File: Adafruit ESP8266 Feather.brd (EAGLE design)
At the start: 50.8 x 22.9 mm, 40 parts, among them IC1 CP2104, Q1 mmbt2222, Q2 mmbt2222, SW2 KMR2, U2 SPX3819, U3 MCP73831T-2ACI/OT, X1 JSTPH, X2 ESP-12, X4 20329

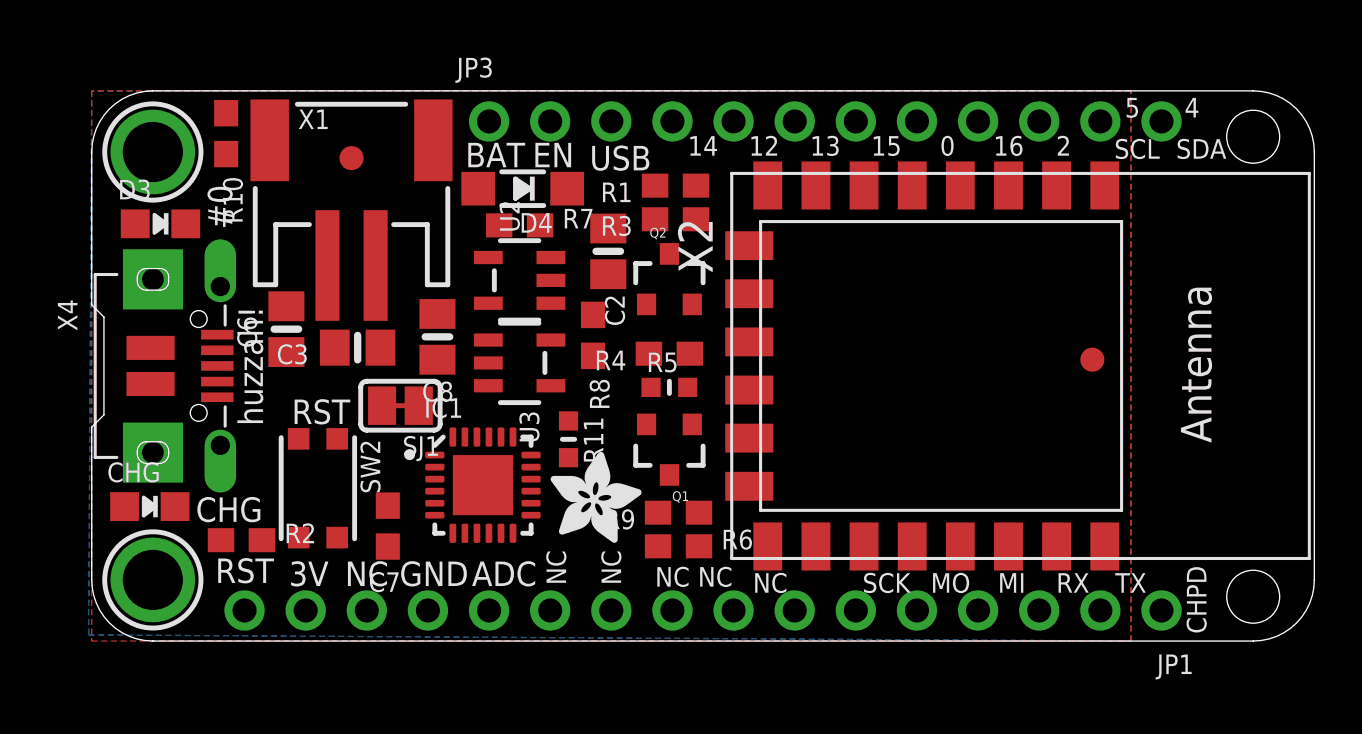
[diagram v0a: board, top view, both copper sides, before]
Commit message: Finished Schematic: CP2104 + SPX3819 + MCP73831T-2ACI/OT + KMR2(Reset)
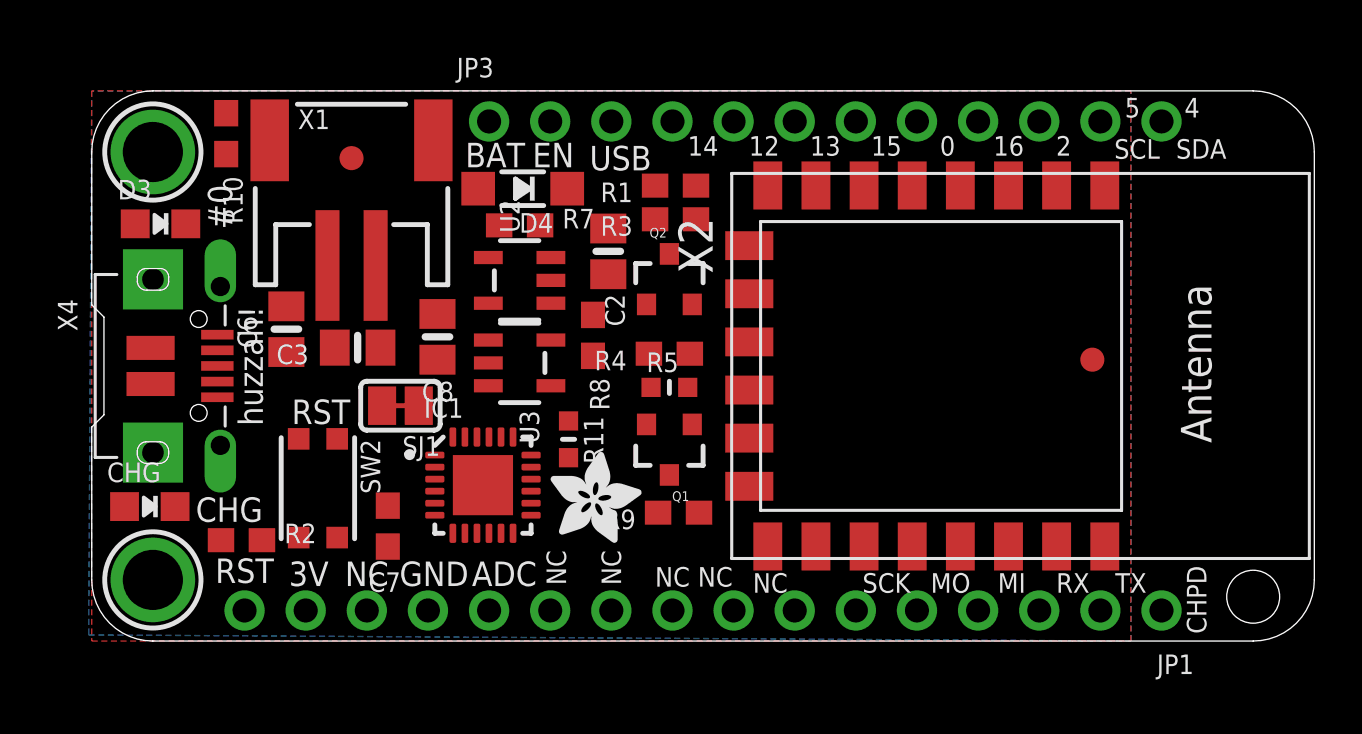
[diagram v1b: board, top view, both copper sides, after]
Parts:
- removed R6: 4.7K, microbuilder:0603-NO
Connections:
- removed net IN: U2.1
- removed net REGIN: IC1.7
- removed net VDD: IC1.6, U3.4
- removed net VIO: IC1.5
- removed net VSS: U3.2
- new net DTR: IC1.23
- new net EN: R7.1, U2.3
- new net GPIO0: R10.1
- new net N$1: CHG.C, R2.1
- new net N$2: IC1.3, X4.D+
- new net N$3: R2.2, U3.1
- new net N$4: R8.1, U3.5
- new net N$6: IC1.4, X4.D-
- new net N$7: SJ1.1, U3.3
- new net RTS: IC1.19
- new net TXD: IC1.20
- new net USB_RX: IC1.21
- new net VCC: X2.8
- net 3.3V: now also C2.1, C7.1, C8.1, D3.A, IC1.5, IC1.6, IC1.7, U2.5; no longer X2.8
- net GND: now also C2.2, C3.2, C6.2, C7.2, C8.2, R8.2, SW2.A, SW2.A', U3.2, X1.1
- net RESET: now also R3.1
- net VBAT: now also C3.1, D4.A, SJ1.2, X1.2; no longer U3.3
- net VBUS: now also C6.1, CHG.A, D4.C, R7.2, U2.1, U3.4

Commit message: Schematic: ESP8266 + (JP1 + JP3 I/O Headers)
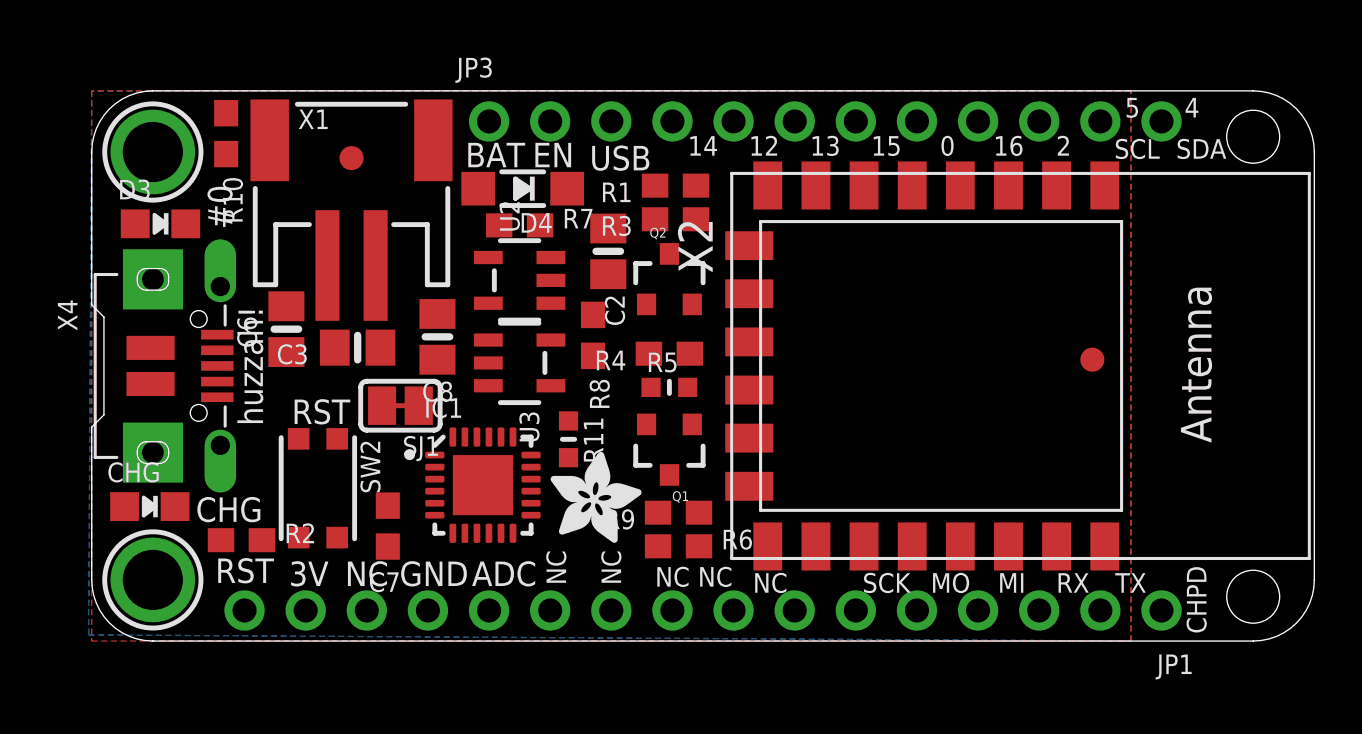
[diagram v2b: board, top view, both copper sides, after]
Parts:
- added R6: 4.7K, microbuilder:0603-NO
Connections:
- removed net VCC: X2.8
- new net ADC: JP1.12, X2.2
- new net CH_PD: JP1.1, R1.1, X2.3
- new net GPIO12/MISO: JP1.4, JP3.5, X2.6
- new net GPIO13/MOSI: JP1.5, JP3.6, X2.7
- new net GPIO14/SCK: JP1.6, JP3.4, X2.5
- new net GPIO15: JP3.7, R6.2, X2.10
- new net GPIO16: JP3.9, X2.4
- new net GPIO2: JP3.10, R9.1, X2.11
- new net GPIO4/SDA: JP3.12, X2.13
- new net GPIO5/SCL: JP3.11, X2.14
- new net N$12: Q1.1, R4.2
- new net N$13: Q2.1, R5.2
- new net RXD: JP1.3, R11.2, X2.15
- net 3.3V: now also JP1.15, R1.2, R9.2, X2.8
- net DTR: now also Q2.2, R4.1
- net EN: now also JP3.2
- net GND: now also JP1.13, R6.1
- net GPIO0: now also JP3.8, Q2.3, X2.12
- net RESET: now also JP1.16, Q1.3, X2.1
- net RTS: now also Q1.2, R5.1
- net TXD: now also JP1.2, X2.16
- net USB_RX: now also R11.1
- net VBAT: now also JP3.1
- net VBUS: now also JP3.3

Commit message: Traces Top: ESP8266 Unrouted
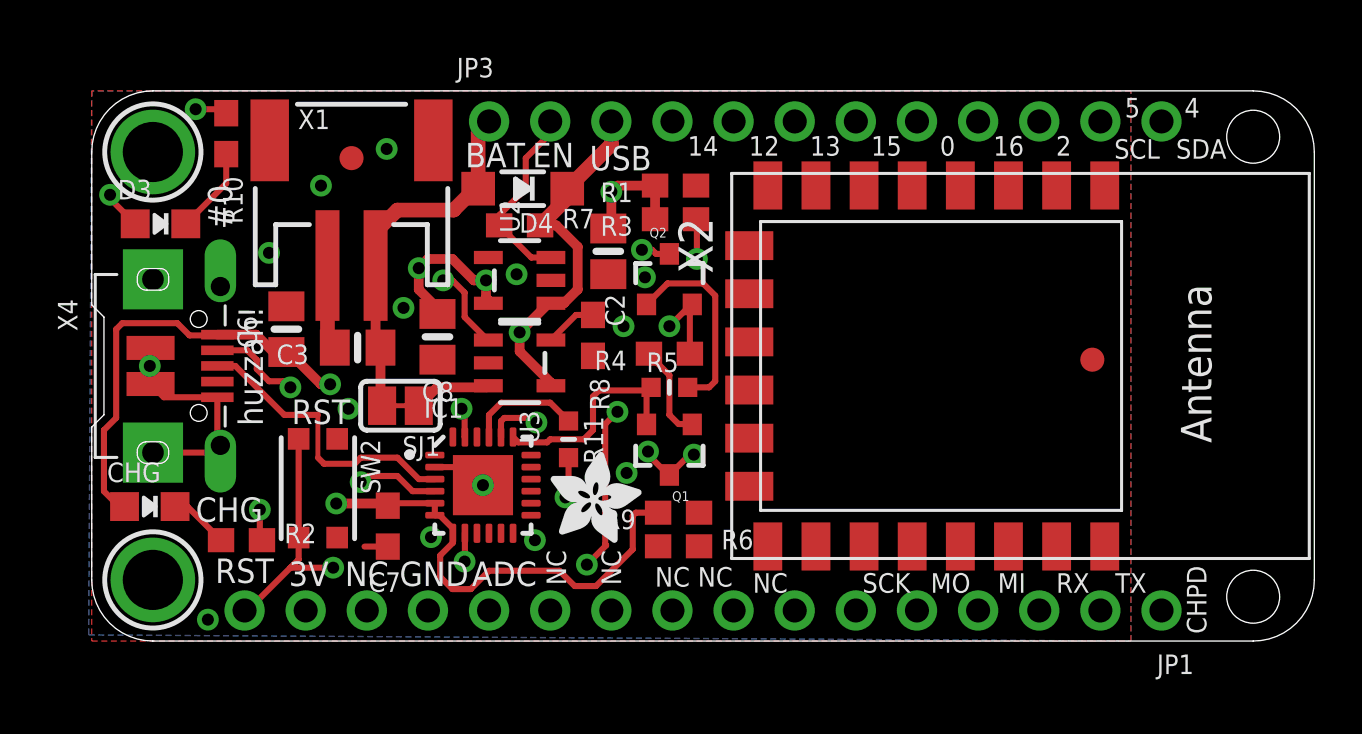
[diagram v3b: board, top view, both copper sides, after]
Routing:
- net VBUS: track 0.00 -> 34.5 mm, vias 0 -> 3
- net 3.3V: track 0.00 -> 32.9 mm, vias 0 -> 5
- net GND: track 0.00 -> 16.7 mm, vias 0 -> 14
- net VBAT: track 0.00 -> 15.5 mm
- net RESET: track 0.00 -> 14.3 mm, vias 0 -> 4
- net N$2: track 0.00 -> 12.2 mm
- net GPIO0: track 0.00 -> 9.46 mm, vias 0 -> 4
- net RTS: track 0.00 -> 9.03 mm
- net N$13: track 0.00 -> 8.23 mm
- net EN: track 0.00 -> 7.90 mm
- net N$6: track 0.00 -> 7.34 mm, vias 0 -> 2
- net N$3: track 0.00 -> 4.80 mm, vias 0 -> 2
- net USB_RX: track 0.00 -> 4.75 mm
- net DTR: track 0.00 -> 4.71 mm, vias 0 -> 2
- net N$12: track 0.00 -> 4.01 mm
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
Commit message: Feather .Brd: minor adjustments
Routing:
- net GPIO0: track 9.46 -> 77.7 mm, vias 4 -> 6
- net RESET: track 14.3 -> 74.4 mm, vias 4 -> 5
- net 3.3V: track 32.9 -> 86.4 mm
- net ADC: track 0.00 -> 44.7 mm, vias 0 -> 1
- net CH_PD: track 0.71 -> 42.4 mm, vias 0 -> 2
- net GPIO14/SCK: track 0.00 -> 34.1 mm, vias 0 -> 1
- net GPIO12/MISO: track 0.00 -> 32.8 mm, vias 0 -> 2
- net TXD: track 2.26 -> 33.3 mm, vias 1 -> 2
- net GPIO2: track 0.13 -> 30.7 mm, vias 0 -> 2
- net RXD: track 1.70 -> 27.6 mm, vias 1 -> 2
- net GPIO15: track 0.29 -> 25.9 mm, vias 0 -> 1
- net GPIO13/MOSI: track 0.00 -> 25.3 mm, vias 0 -> 2
- net VBUS: track 34.5 -> 56.3 mm
- net GPIO4/SDA: track 0.00 -> 21.6 mm, vias 0 -> 1
- net GPIO5/SCL: track 0.00 -> 20.3 mm, vias 0 -> 1
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
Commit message: Feather .Brd: completed the layout design
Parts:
- removed IC1: CP2104, microbuilder:QFN24_4MM_SMSC
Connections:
- net 3.3V: no longer IC1.5, IC1.6, IC1.7
- net CH_PD: no longer X2.3
- net DTR: no longer IC1.23
- net GND: no longer IC1.2, IC1.THERM
- net N$2: no longer IC1.3
- net N$6: no longer IC1.4
- net RTS: no longer IC1.19
- net TXD: no longer IC1.20
- net USB_RX: no longer IC1.21
- net VBUS: no longer IC1.8
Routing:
- net CH_PD: track 42.4 -> 31.5 mm
- net 3.3V: track 86.4 -> 82.7 mm
- net GND: track 16.7 -> 15.0 mm, vias 16 -> 15
- net VBUS: track 56.3 -> 55.1 mm
- net N$6: track 12.5 -> 11.6 mm
- net USB_RX: track 4.75 -> 3.83 mm
- net N$2: track 12.2 -> 11.6 mm
- net TXD: track 33.3 -> 32.7 mm
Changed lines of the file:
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@@
 <attribute name="VALUE" x="5.08" y="19.05" size="0.8128" layer="27" font="vector" ratio="10" rot="R270"/>
-</element>
-<element name="IC1" library="microbuilder" package="QFN24_4MM_SMSC" value="CP2104" x="16.256" y="6.477" smashed="yes">
-<attribute name="NAME" x="13.806" y="9.277" size="0.8128" layer="25" ratio="18"/>
-<attribute name="VALUE" x="14.137" y="5.105" size="0.8128" layer="27" ratio="10"/>
 </element>
 <element name="X4" library="microbuilder" package="4UCONN_20329_V2" value="20329" x="4.445" y="11.43" smashed="yes" rot="R270">
@@
 <contactref element="SW2" pad="A"/>
 <contactref element="SW2" pad="A'"/>
-<contactref element="IC1" pad="2"/>
 <contactref element="X4" pad="SPRT@1"/>
 <contactref element="X4" pad="SPRT@2"/>
@@
 <contactref element="X4" pad="GND"/>
 <contactref element="C2" pad="2"/>
-<contactref element="IC1" pad="THERM"/>
-<wire x1="16.002" y1="7.227" x2="14.256" y2="7.227" width="0.254" layer="1"/>
 <via x="10.668" y="9.652" extent="1-16" drill="0.5"/>
-<via x="16.256" y="6.477" extent="1-16" drill="0.5"/>
 <via x="18.415" y="4.191" extent="1-16" drill="0.5"/>
 <via x="22.225" y="6.985" extent="1-16" drill="0.5"/>
@@
 <wire x1="14.366" y1="11.69" x2="14.366" y2="11.572" width="0.4064" layer="1"/>
 <wire x1="14.366" y1="11.572" x2="14.224" y2="11.43" width="0.4064" layer="1"/>
+<wire x1="21.463" y1="15.2425" x2="22.987" y2="15.113" width="0" layer="19" extent="1-1"/>
+<wire x1="22.098" y1="13.081" x2="22.987" y2="15.113" width="0" layer="19" extent="1-1"/>
+<wire x1="20.828" y1="11.85" x2="22.098" y2="13.081" width="0" layer="19" extent="1-1"/>
+<wire x1="19.0801" y1="14.986" x2="21.463" y2="15.2425" width="0" layer="19" extent="1-1"/>
+<wire x1="17.653" y1="15.24" x2="19.0801" y2="14.986" width="0" layer="19" extent="1-1"/>
+<wire x1="16.4799" y1="11.557" x2="17.653" y2="15.24" width="0" layer="19" extent="1-1"/>
+<wire x1="14.366" y1="11.69" x2="16.4799" y2="11.557" width="0" layer="19" extent="1-1"/>
+<wire x1="12.954" y1="13.843" x2="14.366" y2="11.69" width="0" layer="19" extent="1-1"/>
+<wire x1="10.099" y1="12.192" x2="12.954" y2="13.843" width="0" layer="19" extent="1-1"/>
+<wire x1="8.088" y1="13.909" x2="9.795" y2="15.604" width="0" layer="19" extent="1-1"/>
+<wire x1="7.366" y1="16.129" x2="8.088" y2="13.909" width="0" layer="19" extent="1-1"/>
+<wire x1="5.345" y1="14.73" x2="7.366" y2="16.129" width="0" layer="19" extent="1-1"/>
+<wire x1="10.668" y1="9.652" x2="10.099" y2="12.192" width="0" layer="19" extent="1-1"/>
+<wire x1="10.198" y1="8.4" x2="10.668" y2="9.652" width="0" layer="19" extent="1-1"/>
+<wire x1="2.545" y1="15.03" x2="5.345" y2="14.73" width="0" layer="19" extent="1-1"/>
+<wire x1="2.445" y1="12.18" x2="2.545" y2="15.03" width="0" layer="19" extent="1-1"/>
+<wire x1="2.413" y1="11.43" x2="2.445" y2="12.18" width="0" layer="19" extent="1-1"/>
+<wire x1="2.445" y1="10.68" x2="2.413" y2="11.43" width="0" layer="19" extent="1-1"/>
+<wire x1="9.525" y1="18.923" x2="9.795" y2="15.604" width="0" layer="19" extent="1-1"/>
+<wire x1="12.2555" y1="20.447" x2="9.525" y2="18.923" width="0" layer="19" extent="1-1"/>
+<wire x1="10.198" y1="4.3" x2="10.198" y2="8.4" width="0" layer="19" extent="1-1"/>
+<wire x1="11.335" y1="3.925" x2="10.198" y2="4.3" width="0" layer="19" extent="1-1"/>
+<wire x1="14.097" y1="4.318" x2="12.302" y2="3.925" width="0" layer="19" extent="1-1"/>
+<wire x1="16.256" y1="6.477" x2="14.097" y2="4.318" width="0" layer="19" extent="1-1"/>
+<wire x1="13.97" y1="1.27" x2="14.097" y2="4.318" width="0" layer="19" extent="1-1"/>
+<wire x1="18.415" y1="4.191" x2="16.256" y2="6.477" width="0" layer="19" extent="1-1"/>
+<wire x1="22.225" y1="6.985" x2="18.415" y2="4.191" width="0" layer="19" extent="1-1"/>
+<wire x1="23.534" y1="3.937" x2="22.225" y2="6.985" width="0" layer="19" extent="1-1"/>
+<wire x1="26.797" y1="4.064" x2="23.534" y2="3.937" width="0" layer="19" extent="1-1"/>
+<wire x1="28.092" y1="3.93" x2="26.797" y2="4.064" width="0" layer="19" extent="1-1"/>
+<wire x1="29.591" y1="5.715" x2="28.092" y2="3.93" width="0" layer="19" extent="1-1"/>
+<wire x1="4.826" y1="0.889" x2="10.198" y2="4.3" width="0" layer="19" extent="1-1"/>
 </signal>
 <signal name="VBUS">
@@
 <wire x1="1.016" y1="9.271" x2="1.016" y2="12.954" width="0.254" layer="1"/>
 <wire x1="1.016" y1="12.954" x2="1.27" y2="13.208" width="0.254" layer="1"/>
-<contactref element="IC1" pad="8"/>
 <contactref element="X4" pad="VBUS"/>
 <contactref element="R7" pad="2"/>
-<wire x1="15.506" y1="4.477" x2="15.506" y2="3.29" width="0.254" layer="1"/>
 <wire x1="15.506" y1="3.29" x2="15.494" y2="3.302" width="0.254" layer="1"/>
 <via x="15.494" y="3.302" extent="1-16" drill="0.5"/>
@@
 <via x="13.589" y="15.494" extent="1-16" drill="0.5"/>
 <contactref element="C2" pad="1"/>
-<contactref element="IC1" pad="7"/>
-<contactref element="IC1" pad="6"/>
-<contactref element="IC1" pad="5"/>
 <wire x1="8.89" y1="1.27" x2="8.89" y2="4.826" width="0.4064" layer="16"/>
 <wire x1="23.407" y1="17.526" x2="23.407" y2="18.923" width="0.4064" layer="1"/>
-<wire x1="14.256" y1="5.727" x2="14.256" y2="5.227" width="0.254" layer="1"/>
 <via x="10.16" y="5.715" extent="1-16" drill="0.5"/>
 <wire x1="9.779" y1="5.715" x2="8.89" y2="4.826" width="0.4064" layer="16"/>
@@
 <via x="0.762" y="18.542" extent="1-16" drill="0.5"/>
 <wire x1="0.762" y1="18.542" x2="1.524" y2="17.78" width="0.254" layer="16"/>
-<wire x1="15.006" y1="4.477" x2="15.006" y2="4.084" width="0.254" layer="1"/>
 <wire x1="15.006" y1="4.084" x2="14.478" y2="3.556" width="0.254" layer="1"/>
 <wire x1="14.478" y1="3.556" x2="14.478" y2="2.667" width="0.254" layer="1"/>
@@
 <via x="21.59" y="18.669" extent="1-16" drill="0.5"/>
 <wire x1="1.524" y1="17.78" x2="14.478" y2="17.78" width="0.254" layer="16"/>
-<wire x1="14.256" y1="5.227" x2="14.458" y2="5.227" width="0.254" layer="1"/>
-<wire x1="14.458" y1="5.227" x2="15.006" y2="4.679" width="0.254" layer="1"/>
-<wire x1="15.006" y1="4.679" x2="15.006" y2="4.477" width="0.254" layer="1"/>
 <via x="16.383" y="14.986" extent="1-16" drill="0.5"/>
 <wire x1="13.589" y1="14.605" x2="13.589" y2="15.494" width="0.4064" layer="1"/>
@@
 <wire x1="21.59" y1="16.129" x2="21.59" y2="18.669" width="0.4064" layer="16"/>
 <wire x1="19.812" y1="14.351" x2="21.59" y2="16.129" width="0.4064" layer="16"/>
-<wire x1="14.256" y1="5.727" x2="12.531" y2="5.727" width="0.254" layer="1"/>
 <wire x1="9.779" y1="5.715" x2="10.16" y2="5.715" width="0.4064" layer="16"/>
 <wire x1="16.383" y1="14.2599" x2="16.4799" y2="14.163" width="0.4064" layer="1"/>
@@
 <wire x1="1.8075" y1="17.3355" x2="0.762" y2="18.381" width="0.254" layer="1"/>
 <wire x1="0.762" y1="18.381" x2="0.762" y2="18.542" width="0.254" layer="1"/>
+<wire x1="12.531" y1="5.727" x2="15.006" y2="4.084" width="0" layer="19" extent="1-1"/>
 </signal>
 <signal name="RESET">
@@
 </signal>
 <signal name="CH_PD">
-<contactref element="X2" pad="3"/>
 <contactref element="R1" pad="1"/>
 <contactref element="JP1" pad="1"/>
@@
 <wire x1="25.4" y1="18.923" x2="25.107" y2="18.923" width="0.254" layer="1"/>
 <wire x1="26.67" y1="16.383" x2="26.67" y2="17.78" width="0.254" layer="16"/>
-<wire x1="38.092" y1="18.93" x2="38.092" y2="11.946" width="0.254" layer="1"/>
-<wire x1="38.092" y1="11.946" x2="39.624" y2="10.414" width="0.254" layer="1"/>
-<wire x1="39.624" y1="10.414" x2="39.624" y2="9.144" width="0.254" layer="1"/>
-<wire x1="39.624" y1="9.144" x2="40.005" y2="8.763" width="0.254" layer="1"/>
 <wire x1="40.005" y1="8.763" x2="40.005" y2="8.255" width="0.254" layer="1"/>
 <wire x1="40.005" y1="8.255" x2="43.18" y2="5.08" width="0.254" layer="1"/>
@@
 <contactref element="X2" pad="16"/>
 <contactref element="JP1" pad="2"/>
-<contactref element="IC1" pad="20"/>
-<wire x1="17.006" y1="8.477" x2="17.006" y2="9.132" width="0.254" layer="1"/>
 <wire x1="17.006" y1="9.132" x2="17.145" y2="9.271" width="0.254" layer="1"/>
 <wire x1="17.145" y1="9.271" x2="18.288" y2="9.271" width="0.254" layer="1"/>
@@
 <signal name="N$2">
 <contactref element="X4" pad="D+"/>
-<contactref element="IC1" pad="3"/>
-<wire x1="14.256" y1="6.727" x2="13.593" y2="6.727" width="0.254" layer="1"/>
 <wire x1="13.593" y1="6.727" x2="12.7" y2="7.62" width="0.254" layer="1"/>
 <wire x1="5.22" y1="11.43" x2="5.969" y2="11.43" width="0.254" layer="1"/>
@@
 <signal name="N$6">
 <contactref element="X4" pad="D-"/>
-<contactref element="IC1" pad="4"/>
-<wire x1="13.331" y1="6.227" x2="14.256" y2="6.227" width="0.254" layer="1"/>
 <wire x1="13.331" y1="6.227" x2="12.7" y2="6.858" width="0.254" layer="1"/>
 <wire x1="12.7" y1="6.858" x2="11.43" y2="6.858" width="0.254" layer="1"/>
@@
 </signal>
 <signal name="RTS">
-<contactref element="IC1" pad="19"/>
 <contactref element="R5" pad="1"/>
 <contactref element="Q1" pad="2"/>
-<wire x1="17.506" y1="8.477" x2="17.728" y2="8.255" width="0.254" layer="1"/>
 <wire x1="17.728" y1="8.255" x2="18.923" y2="8.255" width="0.254" layer="1"/>
 <wire x1="18.923" y1="8.255" x2="19.05" y2="8.382" width="0.254" layer="1"/>
@@
 </signal>
 <signal name="DTR">
-<contactref element="IC1" pad="23"/>
 <contactref element="R4" pad="1"/>
 <contactref element="Q2" pad="2"/>
 <wire x1="24.853" y1="11.938" x2="24.853" y2="13.986" width="0.254" layer="1"/>
-<wire x1="15.506" y1="8.477" x2="15.494" y2="8.489" width="0.254" layer="1"/>
 <wire x1="15.494" y1="8.489" x2="15.494" y2="9.525" width="0.254" layer="1"/>
 <wire x1="15.494" y1="9.525" x2="15.367" y2="9.652" width="0.254" layer="1"/>
@@
 <signal name="USB_RX">
 <contactref element="R11" pad="1"/>
-<contactref element="IC1" pad="21"/>
-<wire x1="16.506" y1="8.477" x2="16.506" y2="9.394" width="0.254" layer="1"/>
 <wire x1="17.018" y1="9.906" x2="19.05" y2="9.906" width="0.254" layer="1"/>
 <wire x1="17.018" y1="9.906" x2="16.506" y2="9.394" width="0.254" layer="1"/>
